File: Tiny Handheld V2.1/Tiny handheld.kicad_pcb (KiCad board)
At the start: 2 copper layers, 34.3 x 58.4 mm, 44 parts, among them IC1 BQ21040DBVR, J1 VDisplay/prog1, J2 HDisplay/prog, J3 USB_C_Receptacle_USB2.0, U1 ATtiny85-20P, U2 ATtiny85-20S

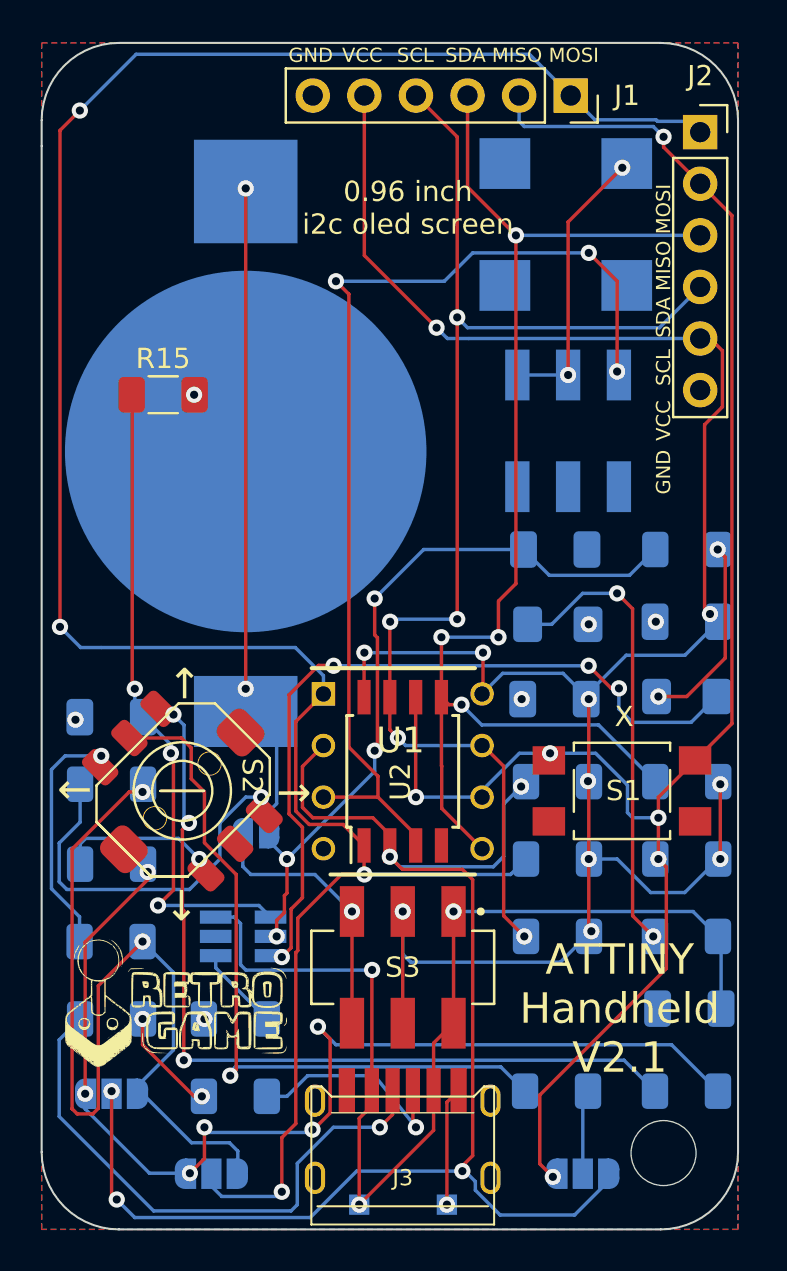
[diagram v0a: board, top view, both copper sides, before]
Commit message: Created smooth traces version of V2.1
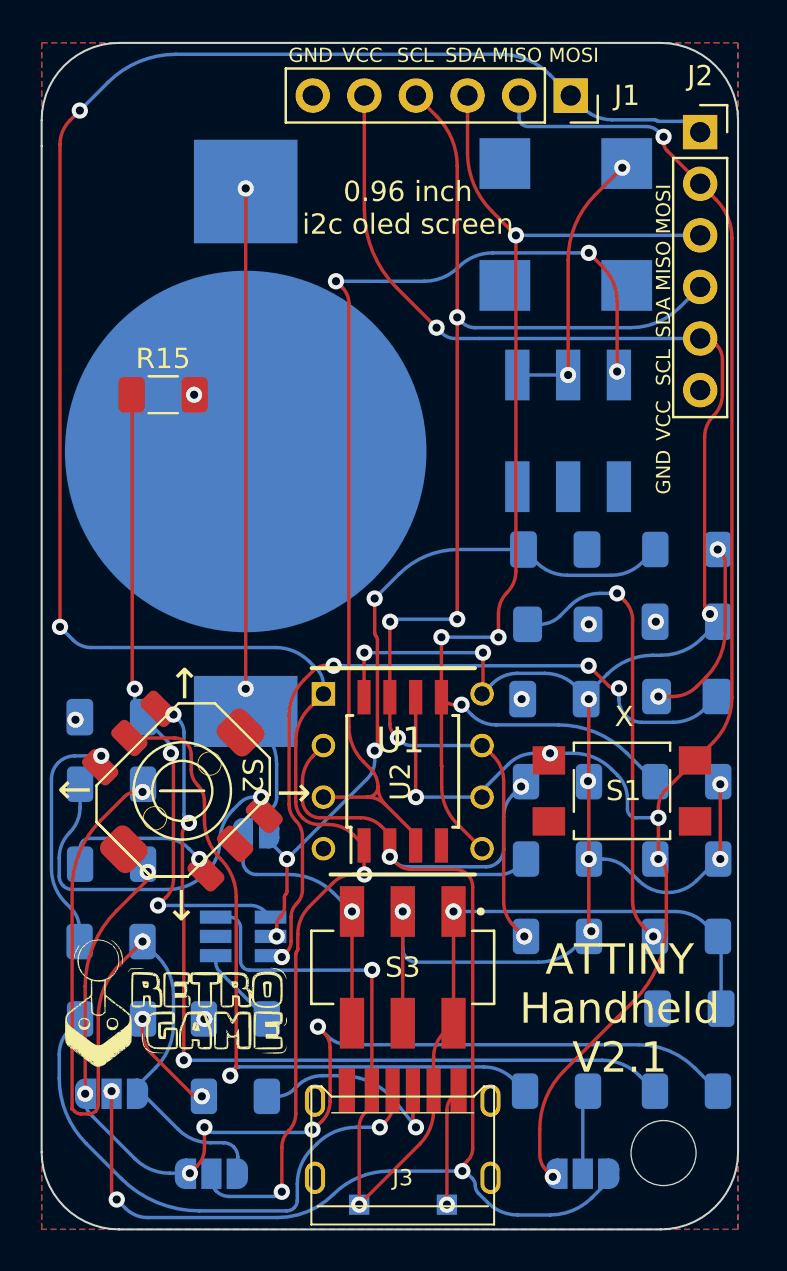
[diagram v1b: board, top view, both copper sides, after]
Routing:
- net PB5/RES: track 116.4 -> 114.8 mm
- net VCC: track 105.9 -> 104.4 mm
- net PB3: track 71.9 -> 70.4 mm
- net PB1/MISO: track 85.9 -> 84.4 mm
- net Net-(JP1-Pad1): track 44.1 -> 43.0 mm
- net Net-(J3-PadA5): track 27.9 -> 27.0 mm
- net Net-(JP1-Pad3): track 54.2 -> 53.3 mm
- net PB2/SCL/SCK: track 63.9 -> 63.1 mm
- net PB0/SDA/MOSI: track 63.4 -> 62.6 mm
- net Net-(D2-Pad1): track 37.5 -> 36.9 mm
- net Net-(C6-Pad1): track 36.3 -> 35.6 mm
- net Net-(R7-Pad2): track 18.3 -> 17.7 mm
- net Net-(R5-Pad2): track 35.7 -> 35.1 mm
- net PB4: track 51.5 -> 52.1 mm
- net ExtVCC: track 54.6 -> 54.0 mm

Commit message: cleanup
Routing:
- net PB5/RES: track 114.8 -> 116.4 mm
- net VCC: track 104.4 -> 105.9 mm
- net PB3: track 70.4 -> 71.9 mm
- net PB1/MISO: track 84.4 -> 85.9 mm
- net Net-(JP1-Pad1): track 43.0 -> 44.1 mm
- net Net-(J3-PadA5): track 27.0 -> 27.9 mm
- net Net-(JP1-Pad3): track 53.3 -> 54.2 mm
- net PB2/SCL/SCK: track 63.1 -> 63.9 mm
- net PB0/SDA/MOSI: track 62.6 -> 63.4 mm
- net Net-(D2-Pad1): track 36.9 -> 37.5 mm
- net Net-(C6-Pad1): track 35.6 -> 36.3 mm
- net Net-(R7-Pad2): track 17.7 -> 18.3 mm
- net Net-(R5-Pad2): track 35.1 -> 35.7 mm
- net PB4: track 52.1 -> 51.5 mm
- net ExtVCC: track 54.0 -> 54.6 mm
